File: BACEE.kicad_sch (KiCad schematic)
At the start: 13 parts, among them U1 24LC1025, U2 24LC1025, U3 DS13375+, U4 ATMEGA328-AU, Y1 32MHz, Y2 16MHz

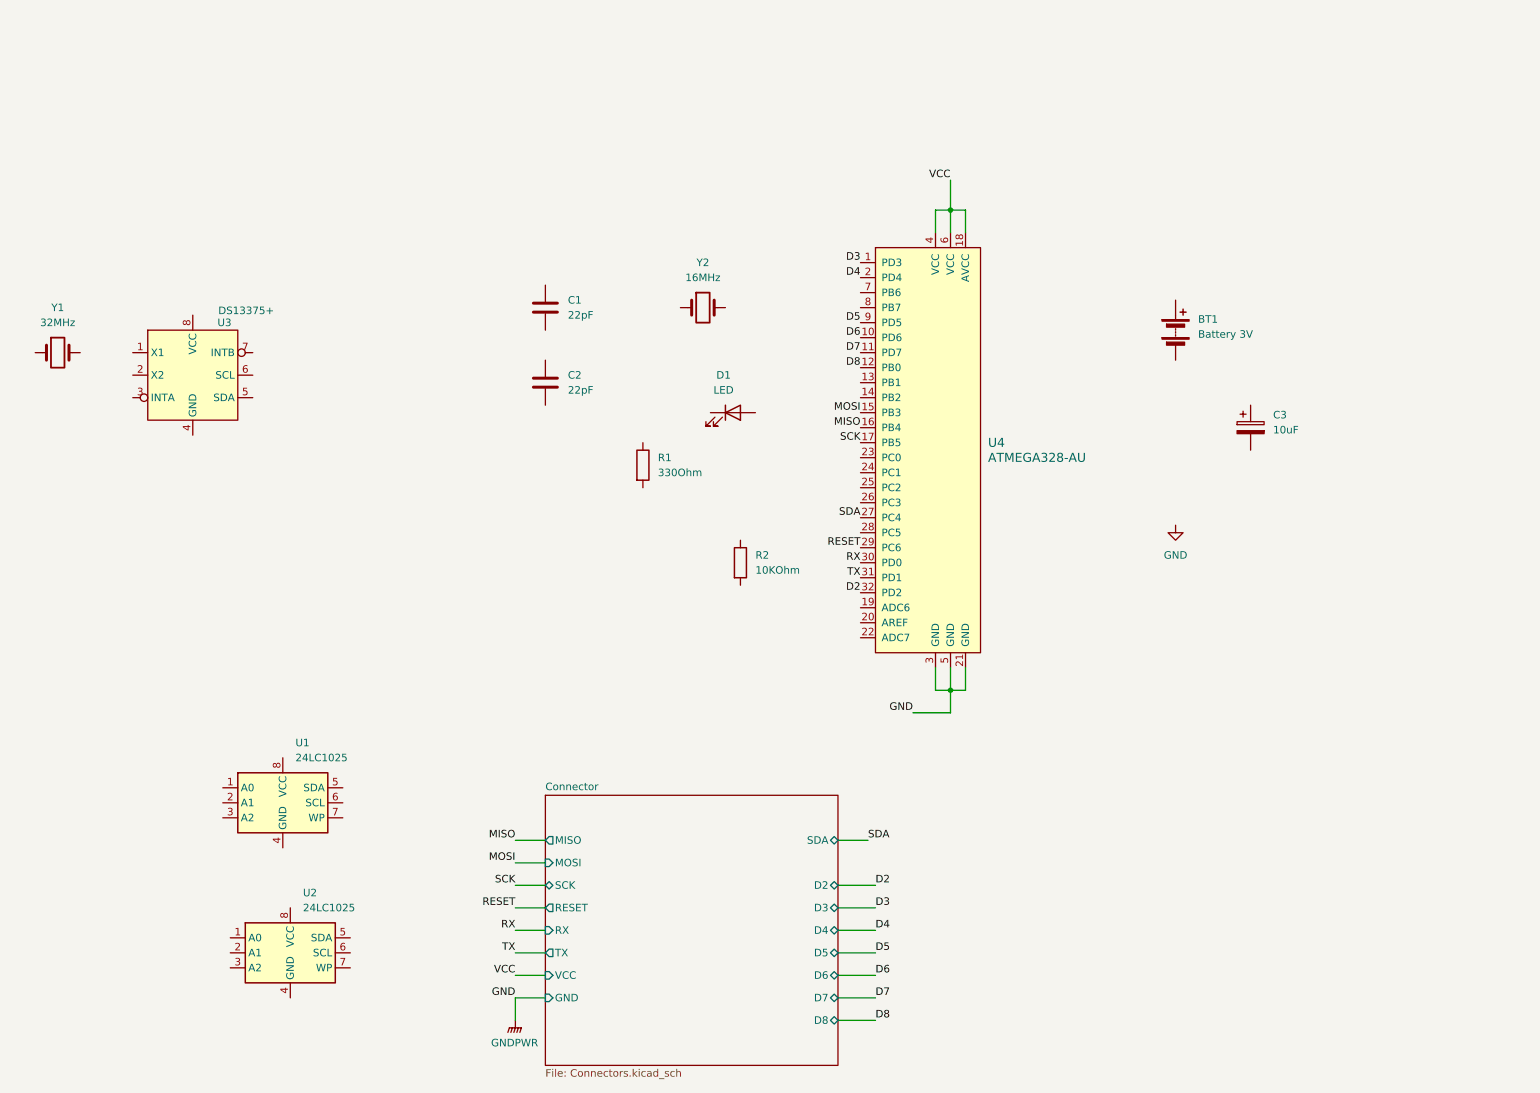
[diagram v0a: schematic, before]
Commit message: Added power flags and corrected the GND
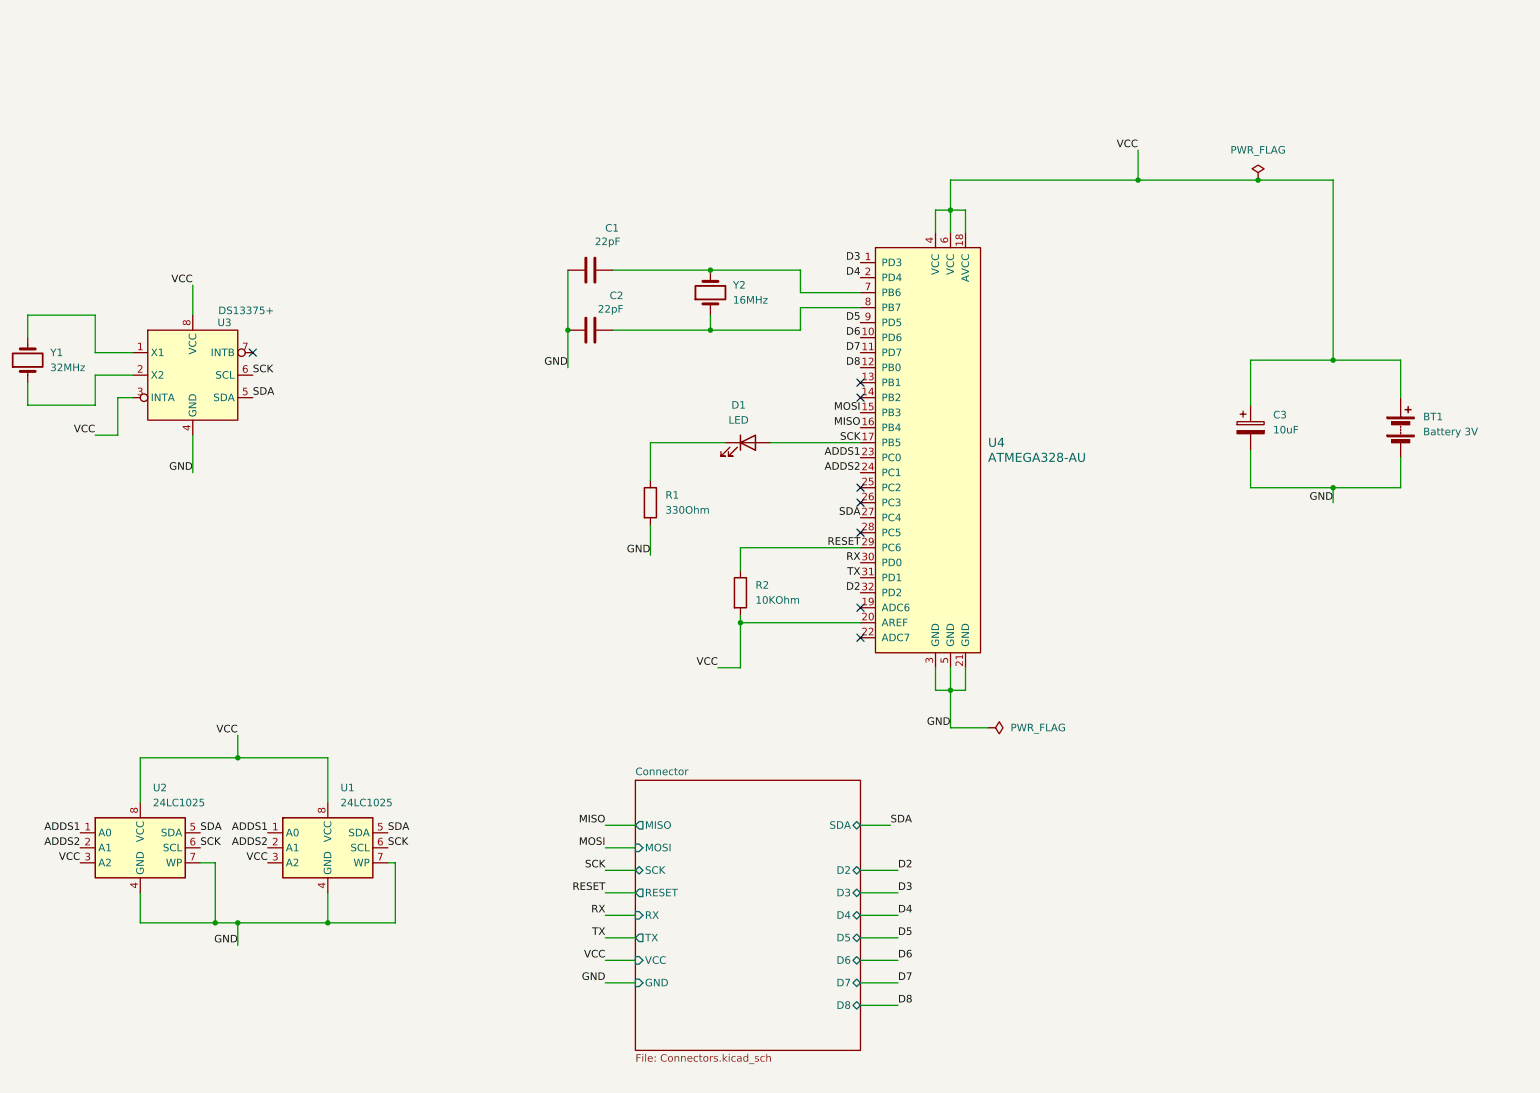
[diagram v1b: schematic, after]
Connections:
- net GND: now also BT1.2 (-), C1.1, C2.1, C3.2, R1.2, U1.4 (GND), U1.7 (WP), U2.4 (GND), U2.7 (WP), U3.4 (GND)
- net RESET: now also R2.1
- net SCK: now also D1.2 (A), U1.6 (SCL), U2.6 (SCL), U3.6 (SCL)
- net SDA: now also U1.5 (SDA), U2.5 (SDA), U3.5 (SDA)
- net VCC: now also BT1.1 (+), C3.1, R2.2, U1.3 (A2), U1.8 (VCC), U2.3 (A2), U2.8 (VCC), U3.3 (INTA), U3.8 (VCC), U4.20 (AREF)
- net ADDS1: now reaches U4.23 (PC0)
- net ADDS1: now also U1.1 (A0), U2.1 (A0)
- net ADDS2: now reaches U4.24 (PC1)
- net ADDS2: now also U1.2 (A1), U2.2 (A1)
- net at U4.7 (PB6): now also C1.2, Y2.2
- net at U4.8 (PB7): now also C2.2, Y2.1
- net at D1.1 (K): now also R1.1
- net at Y1.1: now also U3.2 (X2)
- net at Y1.2: now also U3.1 (X1)
- no-connect marks 0 -> 8
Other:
- moved on the sheet: BT1, C1, C2, D1, R1, R2, U1, U2, Y1, Y2

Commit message: Added functional block descriptions
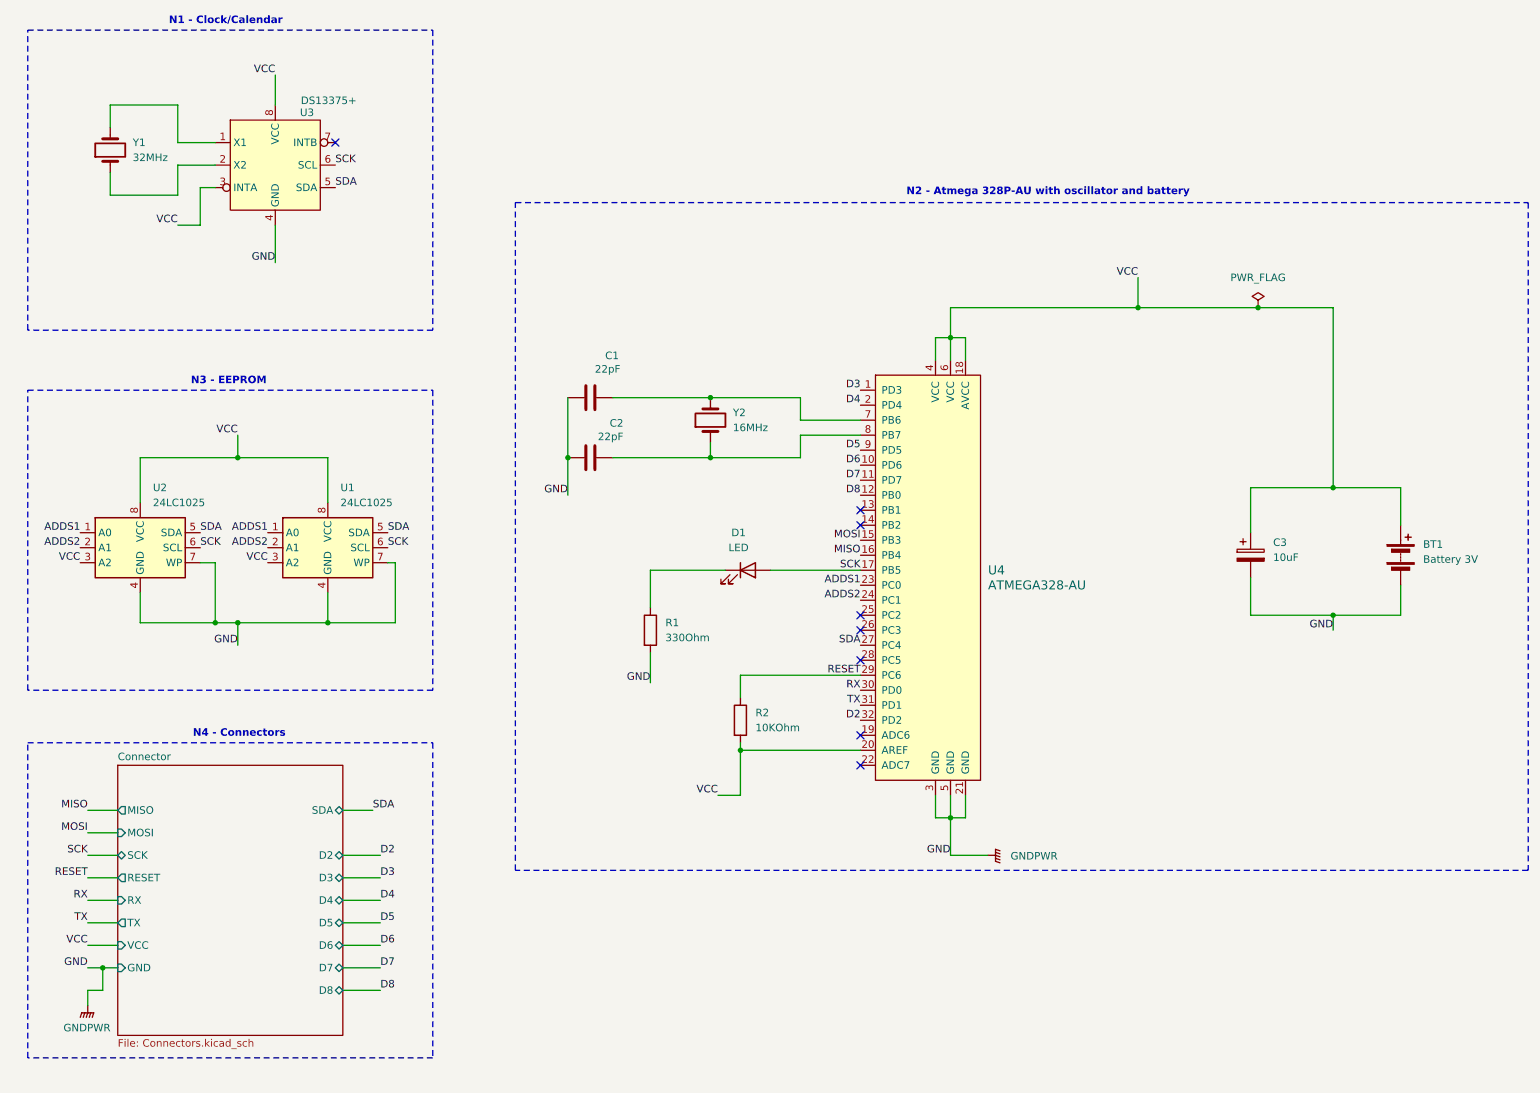
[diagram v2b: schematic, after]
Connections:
- net GND renamed GNDPWR
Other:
- note added: "N1 - Clock/Calendar"
- note added: "N2 - Atmega 328P-AU with oscillator and battery"
- note added: "N3 - EEPROM"
- note added: "N4 - Connectors"
- moved on the sheet: BT1, C1, C2, C3, D1, R1, R2, U1, U2, U3, U4, Y1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
